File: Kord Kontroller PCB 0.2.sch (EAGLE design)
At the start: 190 parts, among them IC2 74HCT1G125DBV, J1 MIDIOUTB, J2 MIDIOUTA, J3 FTSH-105-01-L-DV-KJ, SW2 SPST_TACT-KMR2, U1 AP2112K-3.3, U2 ATSAMD51J19A-AUT, Y1 ECS-.327-12.5-17X-TR

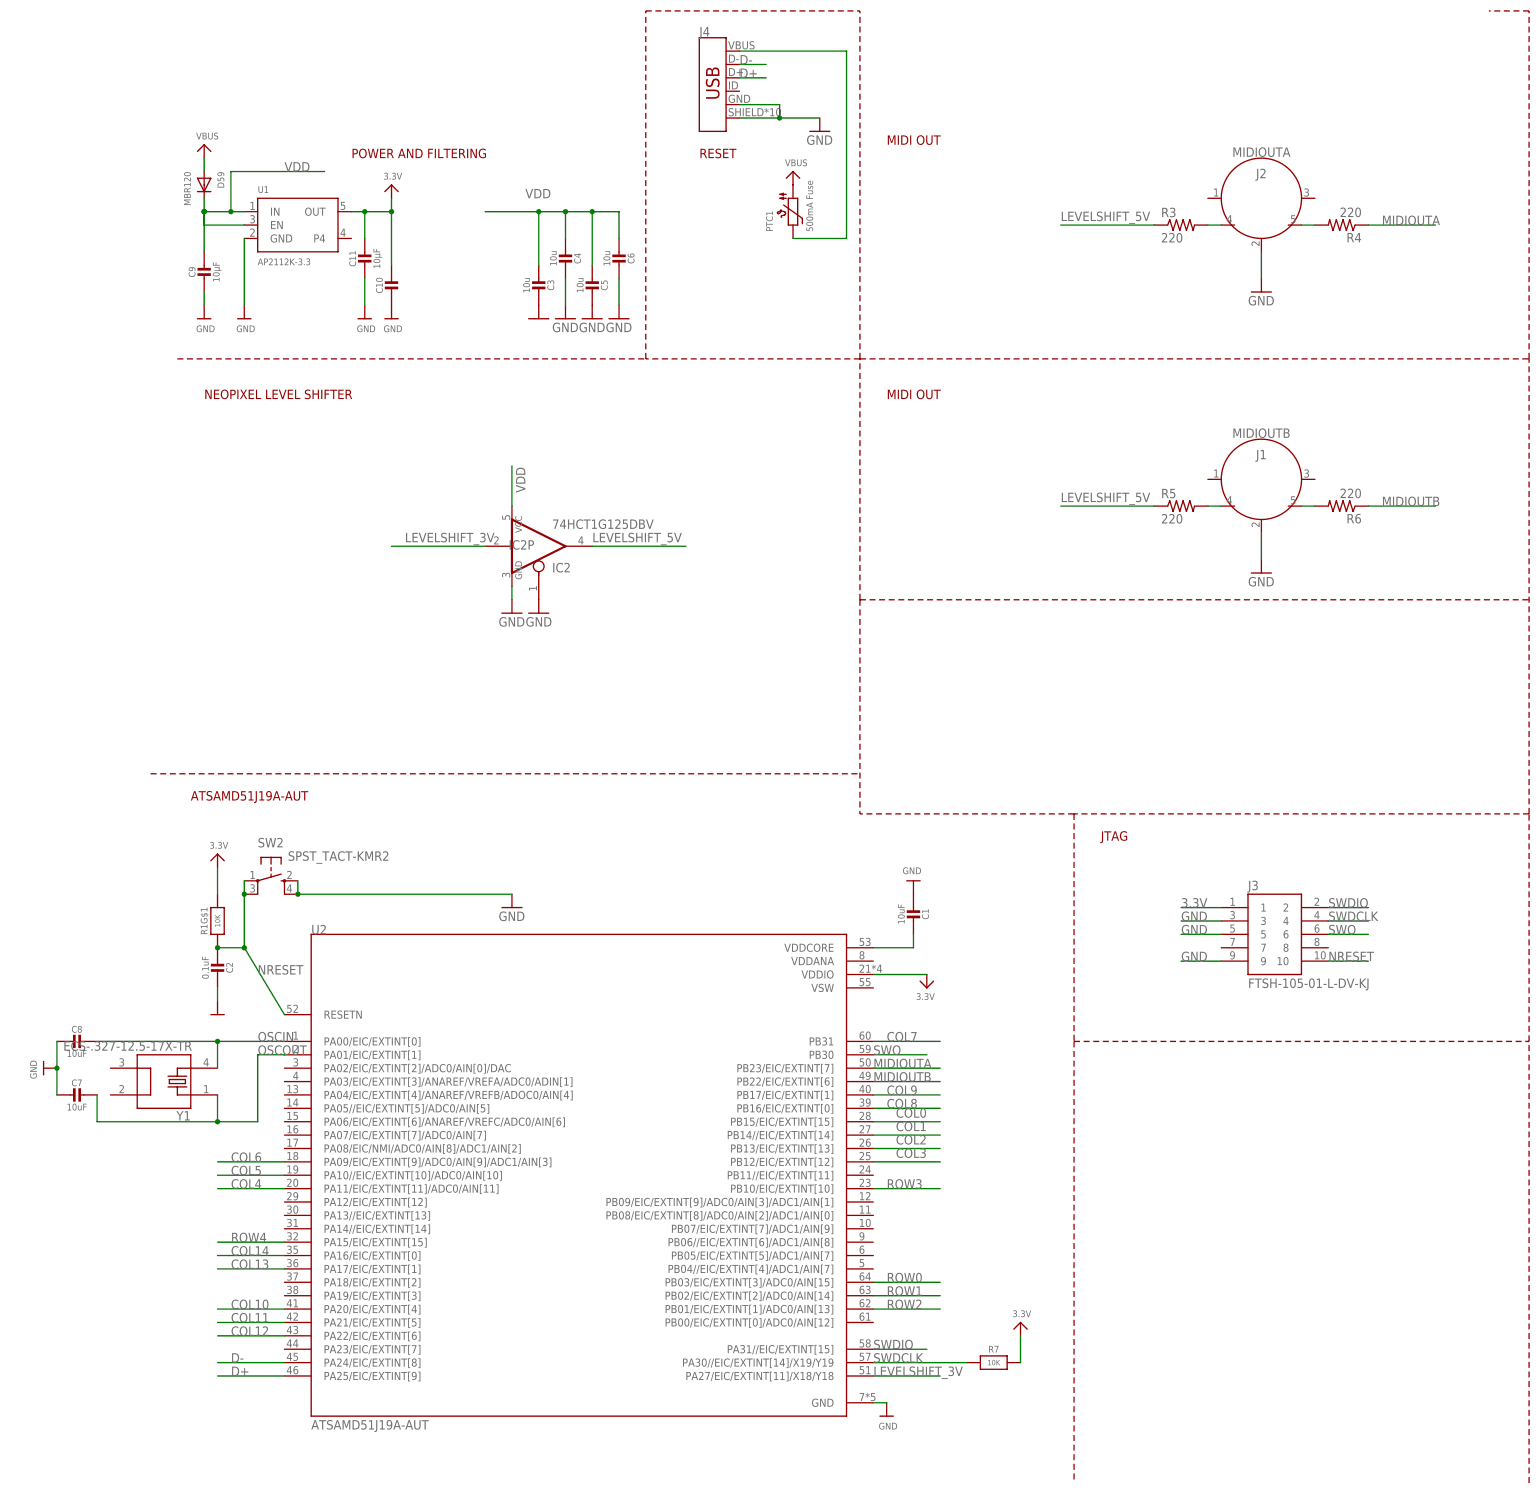
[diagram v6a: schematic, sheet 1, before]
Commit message: Level shifter and decouplers
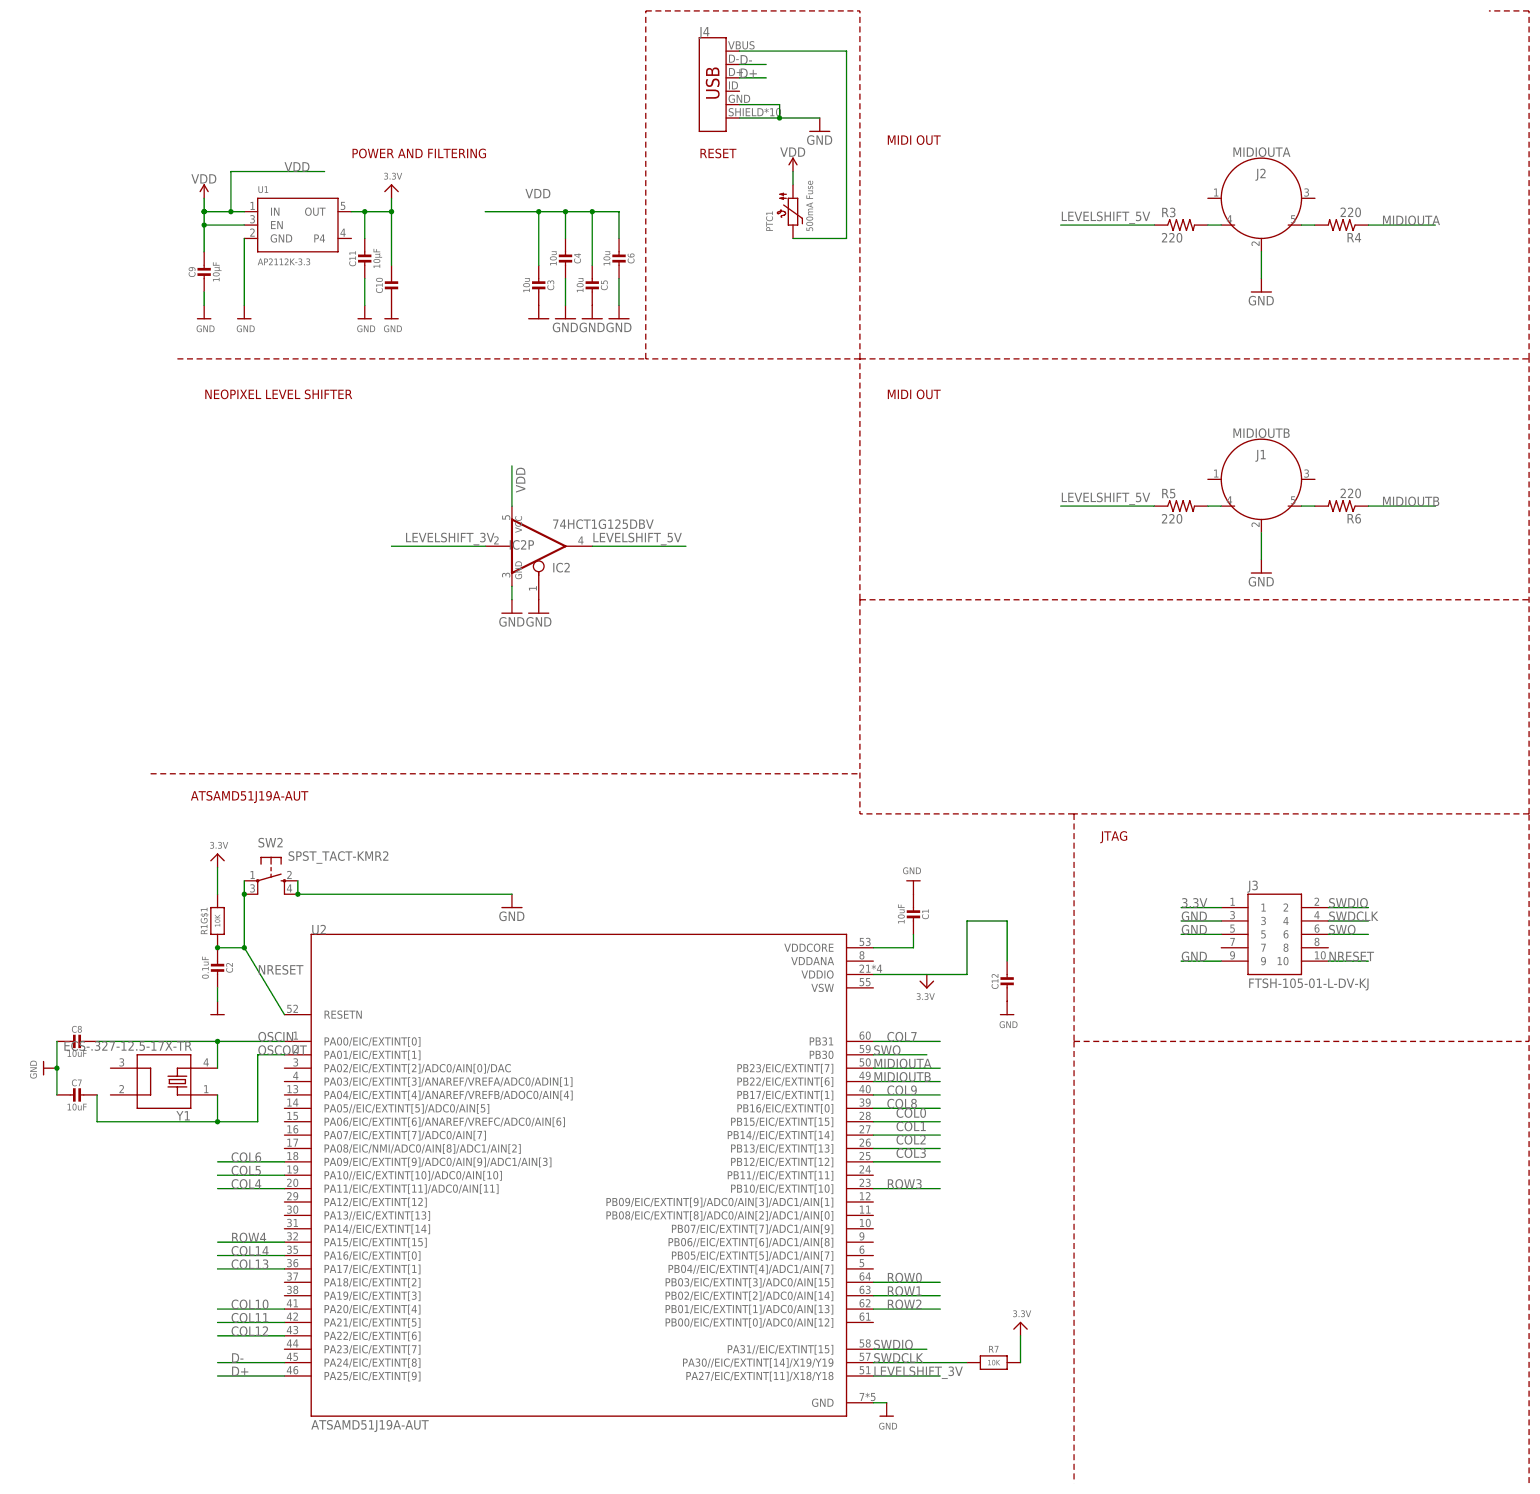
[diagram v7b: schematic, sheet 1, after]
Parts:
- removed D59: MBR120, adafruit:DIODE_SOD-123FL
- added C12: 1uF, microbuilder:CAP_CERAMIC0603_NO
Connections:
- removed net VBUS: D59.A, PTC1.1
- net 3.3V: now also C12.1
- net GND: now also C12.2
- net VDD: now also PTC1.1; no longer D59.C
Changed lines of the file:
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@@
 <?xml version="1.0" encoding="utf-8"?>
 <!DOCTYPE eagle SYSTEM "eagle.dtd">
-<eagle version="9.2.2">
+<eagle version="9.4.2">
 <drawing>
 <settings>
@@
 <part name="U$52" library="microbuilder" deviceset="GND" device=""/>
 <part name="U$53" library="microbuilder" deviceset="GND" device=""/>
-<part name="U$56" library="microbuilder" deviceset="VBUS" device=""/>
-<part name="U$57" library="microbuilder" deviceset="VBUS" device=""/>
 <part name="U1" library="microbuilder" deviceset="VREG_SOT23-5" device="" value="AP2112K-3.3"/>
-<part name="D59" library="adafruit" deviceset="DIODE" device="_SOD-123FL" value="MBR120"/>
 <part name="U$13" library="microbuilder" deviceset="3.3V" device=""/>
 <part name="PTC1" library="microbuilder" deviceset="PTC" device="1206" value="500mA Fuse"/>
@@
 <part name="GND2" library="supply1" deviceset="GND" device=""/>
 <part name="Y1" library="ECS-.327-12.5-17X-TR" deviceset="ECS-.327-12.5-17X-TR" device=""/>
+<part name="SUPPLY1" library="SparkFun-PowerSymbols" deviceset="VDD" device=""/>
+<part name="SUPPLY2" library="SparkFun-PowerSymbols" deviceset="VDD" device=""/>
+<part name="C12" library="microbuilder" deviceset="CAP_CERAMIC" device="0603_NO" value="1uF"/>
+<part name="U$2" library="microbuilder" deviceset="GND" device=""/>
 </parts>
 <sheets>
@@
 <attribute name="VALUE" x="656.336" y="111.76" size="1.27" layer="96"/>
 </instance>
-<instance part="U$56" gate="G$1" x="762" y="142.24" smashed="yes">
-<attribute name="VALUE" x="760.476" y="143.256" size="1.27" layer="96"/>
-</instance>
-<instance part="U$57" gate="G$1" x="650.24" y="147.32" smashed="yes">
-<attribute name="VALUE" x="648.716" y="148.336" size="1.27" layer="96"/>
-</instance>
 <instance part="U1" gate="G$1" x="668.02" y="132.08" smashed="yes">
 <attribute name="NAME" x="660.4" y="138.176" size="1.27" layer="95"/>
 <attribute name="VALUE" x="660.4" y="124.46" size="1.27" layer="95"/>
 </instance>
-<instance part="D59" gate="G$1" x="650.24" y="139.7" smashed="yes" rot="R270">
-<attribute name="NAME" x="652.78" y="142.24" size="1.27" layer="95" rot="R270"/>
-<attribute name="VALUE" x="646.43" y="142.24" size="1.27" layer="96" rot="R270"/>
-</instance>
 <instance part="U$13" gate="G$1" x="685.8" y="139.7" smashed="yes">
 <attribute name="VALUE" x="684.276" y="140.716" size="1.27" layer="96"/>
@@
 <attribute name="NAME" x="647.71686875" y="-36.086559375" size="1.783909375" layer="95" rot="R180"/>
 <attribute name="VALUE" x="647.964559375" y="-22.84491875" size="1.78151875" layer="96" rot="R180"/>
+</instance>
+<instance part="SUPPLY1" gate="VDD" x="762" y="142.24" smashed="yes">
+<attribute name="VALUE" x="762" y="145.034" size="1.778" layer="96" align="bottom-center"/>
+</instance>
+<instance part="SUPPLY2" gate="VDD" x="650.24" y="137.16" smashed="yes">
+<attribute name="VALUE" x="650.24" y="139.954" size="1.778" layer="96" align="bottom-center"/>
+</instance>
+<instance part="C12" gate="G$1" x="802.64" y="-12.7" smashed="yes">
+<attribute name="NAME" x="800.35" y="-11.45" size="1.27" layer="95" font="vector" rot="R90" align="center"/>
+</instance>
+<instance part="U$2" gate="G$1" x="802.64" y="-17.78" smashed="yes">
+<attribute name="VALUE" x="801.116" y="-20.32" size="1.27" layer="96"/>
 </instance>
 </instances>
@@
 <junction x="759.46" y="152.4"/>
 <pinref part="GND2" gate="1" pin="GND"/>
+</segment>
+<segment>
+<pinref part="C12" gate="G$1" pin="2"/>
+<pinref part="U$2" gate="G$1" pin="GND"/>
 </segment>
 </net>
@@
 </segment>
 <segment>
-<wire x1="777.24" y1="-10.16" x2="787.4" y2="-10.16" width="0.1524" layer="91"/>
 <pinref part="U$6" gate="G$1" pin="3.3V"/>
 <pinref part="U2" gate="G$1" pin="VDDIO"/>
+<wire x1="777.24" y1="-10.16" x2="787.4" y2="-10.16" width="0.1524" layer="91"/>
+<wire x1="787.4" y1="-10.16" x2="795.02" y2="-10.16" width="0.1524" layer="91"/>
+<wire x1="795.02" y1="-10.16" x2="795.02" y2="0" width="0.1524" layer="91"/>
+<pinref part="C12" gate="G$1" pin="1"/>
+<wire x1="802.64" y1="0" x2="802.64" y2="-7.62" width="0.1524" layer="91"/>
+<wire x1="795.02" y1="0" x2="802.64" y2="0" width="0.1524" layer="91"/>
 </segment>
 <segment>
@@
 <pinref part="C9" gate="G$1" pin="1"/>
 <wire x1="657.86" y1="134.62" x2="655.32" y2="134.62" width="0.1524" layer="91"/>
-<wire x1="650.24" y1="134.62" x2="650.24" y2="127" width="0.1524" layer="91"/>
 <pinref part="U1" gate="G$1" pin="IN"/>
 <junction x="650.24" y="134.62"/>
-<pinref part="D59" gate="G$1" pin="C"/>
+<wire x1="650.24" y1="132.08" x2="650.24" y2="127" width="0.1524" layer="91"/>
 <wire x1="650.24" y1="134.62" x2="650.24" y2="137.16" width="0.1524" layer="91"/>
 <junction x="650.24" y="134.62"/>
@@
 <junction x="655.32" y="134.62"/>
 <wire x1="650.24" y1="132.08" x2="650.24" y2="134.62" width="0.1524" layer="91"/>
+<junction x="650.24" y="132.08"/>
+<pinref part="SUPPLY2" gate="VDD" pin="VDD"/>
 </segment>
 <segment>
@@
 <label x="711.2" y="81.28" size="1.778" layer="95" rot="R90"/>
 </segment>
-</net>
-<net name="VBUS" class="0">
-<segment>
-<pinref part="U$57" gate="G$1" pin="VBUS"/>
-<pinref part="D59" gate="G$1" pin="A"/>
-<wire x1="650.24" y1="144.78" x2="650.24" y2="142.24" width="0.1524" layer="91"/>
-</segment>
 <segment>
 <pinref part="PTC1" gate="G$1" pin="1"/>
-<pinref part="U$56" gate="G$1" pin="VBUS"/>
-</segment>
-</net>
+<wire x1="762" y1="139.7" x2="762" y2="142.24" width="0.1524" layer="91"/>
+<pinref part="SUPPLY1" gate="VDD" pin="VDD"/>
+</segment>
+</net>

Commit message: Rerouted, gave better routes, switched voltage shifter part
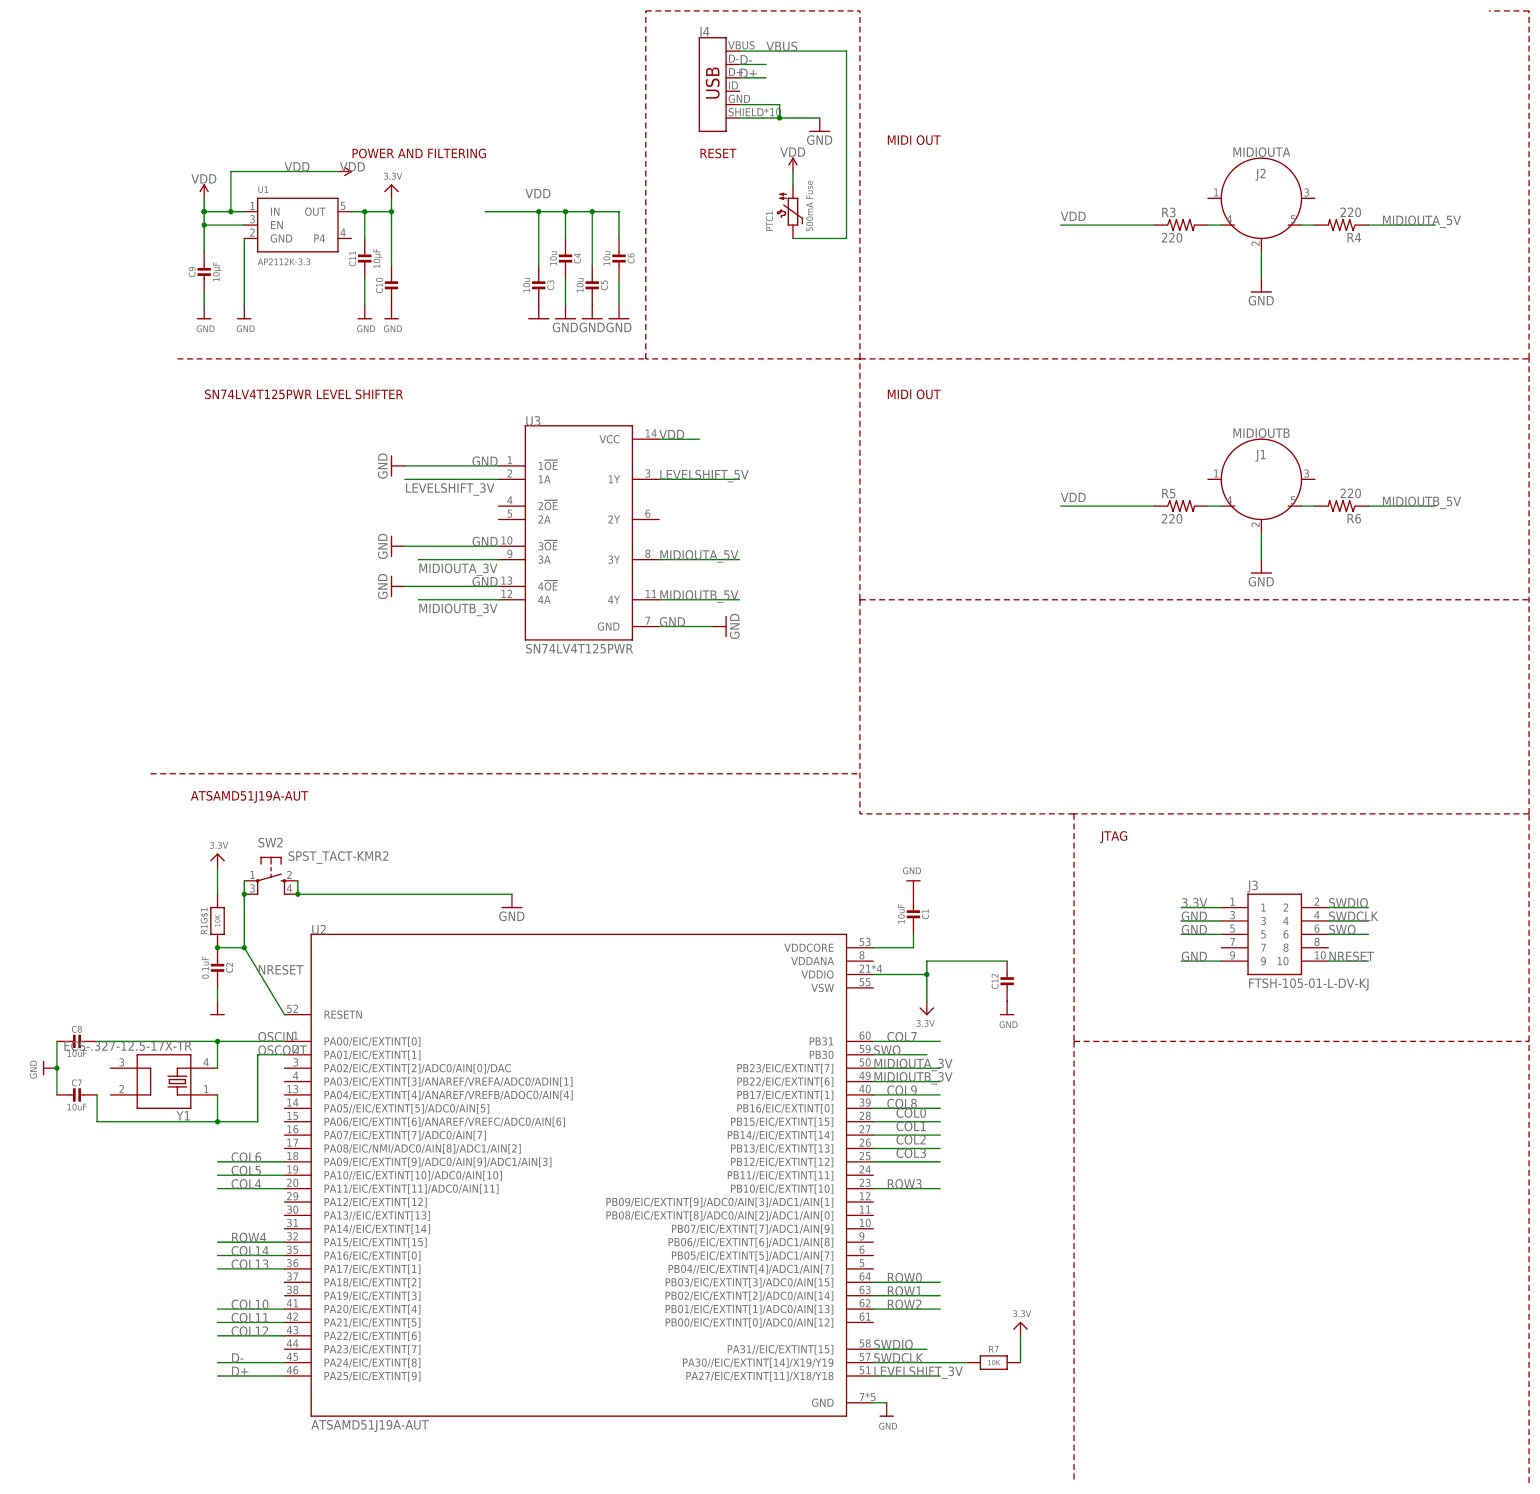
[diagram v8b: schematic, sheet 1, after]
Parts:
- removed IC2: 74HCT1G125DBV, 74xx-little-us:74AHC1G125DBV
- added U3: SN74LV4T125PWR, SN74LV4T125PWR:SN74LV4T125PWR
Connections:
- net N$66 renamed VBUS
- removed net MIDIOUTA: R4.1, U2.PB23/EIC/EXTINT[7]
- removed net MIDIOUTB: R6.1, U2.PB22/EIC/EXTINT[6]
- new net MIDIOUTA_3V: U2.PB23/EIC/EXTINT[7], U3.3A
- new net MIDIOUTA_5V: R4.1, U3.3Y
- new net MIDIOUTB_3V: U2.PB22/EIC/EXTINT[6], U3.4A
- new net MIDIOUTB_5V: R6.1, U3.4Y
- net GND: now also U3.1!OE, U3.3!OE, U3.4!OE, U3.GND; no longer IC2A.OE, IC2P.GND
- net LEVELSHIFT_3V: now also U3.1A; no longer IC2A.I
- net LEVELSHIFT_5V: now also U3.1Y; no longer IC2A.O, R3.1, R5.1
- net VDD: now also R3.1, R5.1, U3.VCC; no longer IC2P.VCC
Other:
- note added: "SN74LV4T125PWR LEVEL SHIFTER"
- note removed: "NEOPIXEL LEVEL SHIFTER"
